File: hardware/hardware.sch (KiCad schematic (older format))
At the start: 1 part, among them P1 CONN_13X2

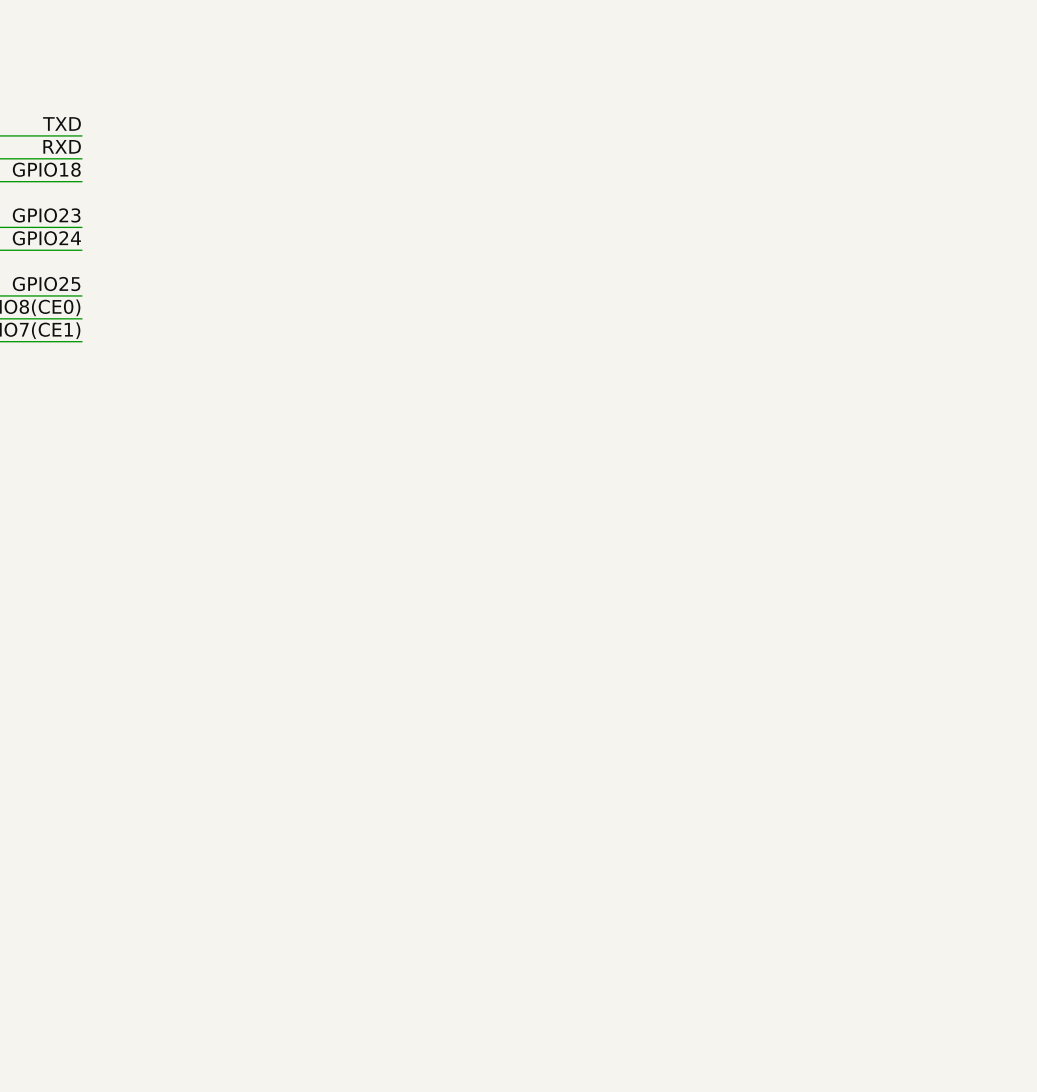
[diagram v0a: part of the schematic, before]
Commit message: Start daughterboard work
What I plan to do here is use the Pi's serial interface to provide the
position value for the servos and then use the other GPIO pins to provide
the selection for which motor is to move.

Signed-off-by: Nkeck720 <noahkeck72@gmail.com>
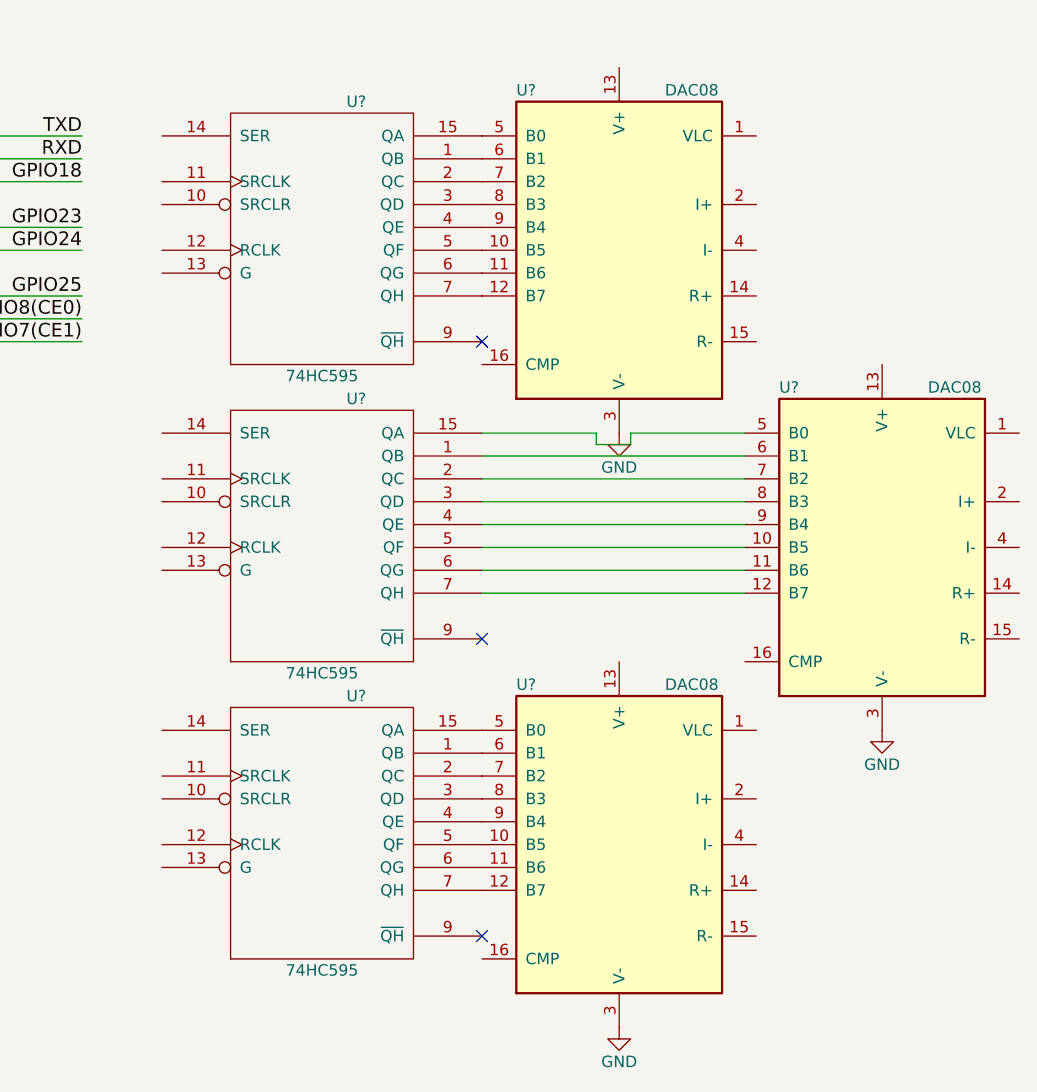
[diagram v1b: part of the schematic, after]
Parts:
- added U? (x3): 74HC595, symbol 74HC595
- added U? (x3): DAC08, symbol DAC08
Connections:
- net GND: now also U?.3 (V-), U?.3 (V-), U?.3 (V-), U?.8 (GND), U?.8 (GND), U?.8 (GND)
- new net: U?.1 (QB), U?.6 (B1) (x3)
- new net: U?.15 (QA), U?.5 (B0) (x3)
- new net: U?.2 (QC), U?.7 (B2) (x3)
- new net: U?.3 (QD), U?.8 (B3) (x3)
- new net: U?.4 (QE), U?.9 (B4) (x3)
- new net: U?.10 (B5), U?.5 (QF) (x3)
- new net: U?.11 (B6), U?.6 (QG) (x3)
- new net: U?.12 (B7), U?.7 (QH) (x3)
- new net VCC: U?.16 (VCC), U?.16 (VCC), U?.16 (VCC)
- no-connect marks 6 -> 9
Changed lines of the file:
@@
 Text GLabel 2900 1050 2    60   Input ~ 0
 +5
+$Comp
+L 74HC595 U?
+U 1 1 59263A27
+P 4550 1950
+F 0 "U?" H 4700 2550 50  0000 C CNN
+F 1 "74HC595" H 4550 1350 50  0000 C CNN
+F 2 "" H 4550 1950 50  0000 C CNN
+F 3 "" H 4550 1950 50  0000 C CNN
+	1    4550 1950
+	1    0    0    -1
+$EndComp
+$Comp
+L 74HC595 U?
+U 1 1 59263B0C
+P 4550 3250
+F 0 "U?" H 4700 3850 50  0000 C CNN
+F 1 "74HC595" H 4550 2650 50  0000 C CNN
+F 2 "" H 4550 3250 50  0000 C CNN
+F 3 "" H 4550 3250 50  0000 C CNN
+	1    4550 3250
+	1    0    0    -1
+$EndComp
+$Comp
+L 74HC595 U?
+U 1 1 59263BC3
+P 4550 4550
+F 0 "U?" H 4700 5150 50  0000 C CNN
+F 1 "74HC595" H 4550 3950 50  0000 C CNN
+F 2 "" H 4550 4550 50  0000 C CNN
+F 3 "" H 4550 4550 50  0000 C CNN
+	1    4550 4550
+	1    0    0    -1
+$EndComp
+$Comp
+L DAC08 U?
+U 1 1 59263EBB
+P 5850 2000
+F 0 "U?" H 5400 2700 50  0000 L CNN
+F 1 "DAC08" H 6050 2700 50  0000 L CNN
+F 2 "" H 5850 2000 50  0000 C CNN
+F 3 "" H 5850 2000 50  0000 C CNN
+	1    5850 2000
+	1    0    0    -1
+$EndComp
+$Comp
+L DAC08 U?
+U 1 1 592640B3
+P 7000 3300
+F 0 "U?" H 6550 4000 50  0000 L CNN
+F 1 "DAC08" H 7200 4000 50  0000 L CNN
+F 2 "" H 7000 3300 50  0000 C CNN
+F 3 "" H 7000 3300 50  0000 C CNN
+	1    7000 3300
+	1    0    0    -1
+$EndComp
+$Comp
+L DAC08 U?
+U 1 1 5926437E
+P 5850 4600
+F 0 "U?" H 5400 5300 50  0000 L CNN
+F 1 "DAC08" H 6050 5300 50  0000 L CNN
+F 2 "" H 5850 4600 50  0000 C CNN
+F 3 "" H 5850 4600 50  0000 C CNN
+	1    5850 4600
+	1    0    0    -1
+$EndComp
+Wire Wire Line
+	5250 2800 5750 2800
+Wire Wire Line
+	5750 2800 5750 2850
+Wire Wire Line
+	5750 2850 5900 2850
+Wire Wire Line
+	5900 2850 5900 2800
+Wire Wire Line
+	5900 2800 6400 2800
+Wire Wire Line
+	5250 2900 6400 2900
+Wire Wire Line
+	5250 3000 6400 3000
+Wire Wire Line
+	6400 3100 5250 3100
+Wire Wire Line
+	5250 3200 6400 3200
+Wire Wire Line
+	6400 3300 5250 3300
+Wire Wire Line
+	6400 3400 5250 3400
+Wire Wire Line
+	5250 3500 6400 3500
+$Comp
+L GND #PWR?
+U 1 1 59264B0C
+P 5850 2800
+F 0 "#PWR?" H 5850 2550 50  0001 C CNN
+F 1 "GND" H 5850 2650 50  0000 C CNN
+F 2 "" H 5850 2800 50  0000 C CNN
+F 3 "" H 5850 2800 50  0000 C CNN
+	1    5850 2800
+	1    0    0    -1
+$EndComp
+$Comp
+L GND #PWR?
+U 1 1 59264B9E
+P 7000 4100
+F 0 "#PWR?" H 7000 3850 50  0001 C CNN
+F 1 "GND" H 7000 3950 50  0000 C CNN
+F 2 "" H 7000 4100 50  0000 C CNN
+F 3 "" H 7000 4100 50  0000 C CNN
+	1    7000 4100
+	1    0    0    -1
+$EndComp
+$Comp
+L GND #PWR?
+U 1 1 59264C45
+P 5850 5400
+F 0 "#PWR?" H 5850 5150 50  0001 C CNN
+F 1 "GND" H 5850 5250 50  0000 C CNN
+F 2 "" H 5850 5400 50  0000 C CNN
+F 3 "" H 5850 5400 50  0000 C CNN
+	1    5850 5400
+	1    0    0    -1
+$EndComp
+NoConn ~ 5250 5000
+NoConn ~ 5250 3700
+NoConn ~ 5250 2400
 $EndSCHEMATC

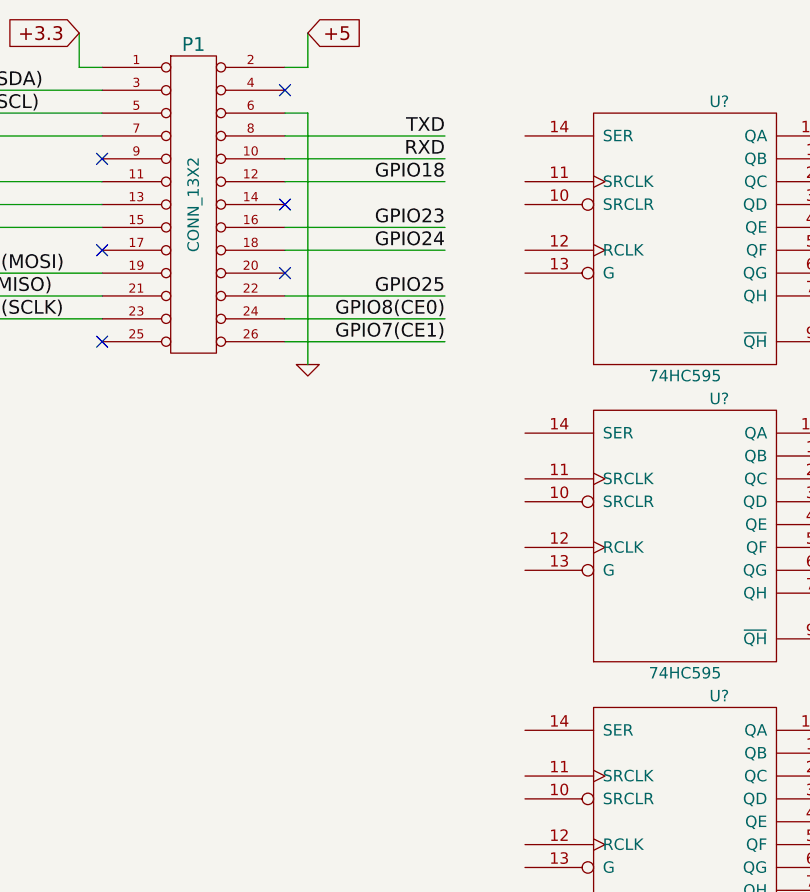
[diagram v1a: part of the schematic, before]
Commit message: Add serial outputs
Signed-off-by: Nkeck720 <noahkeck72@gmail.com>
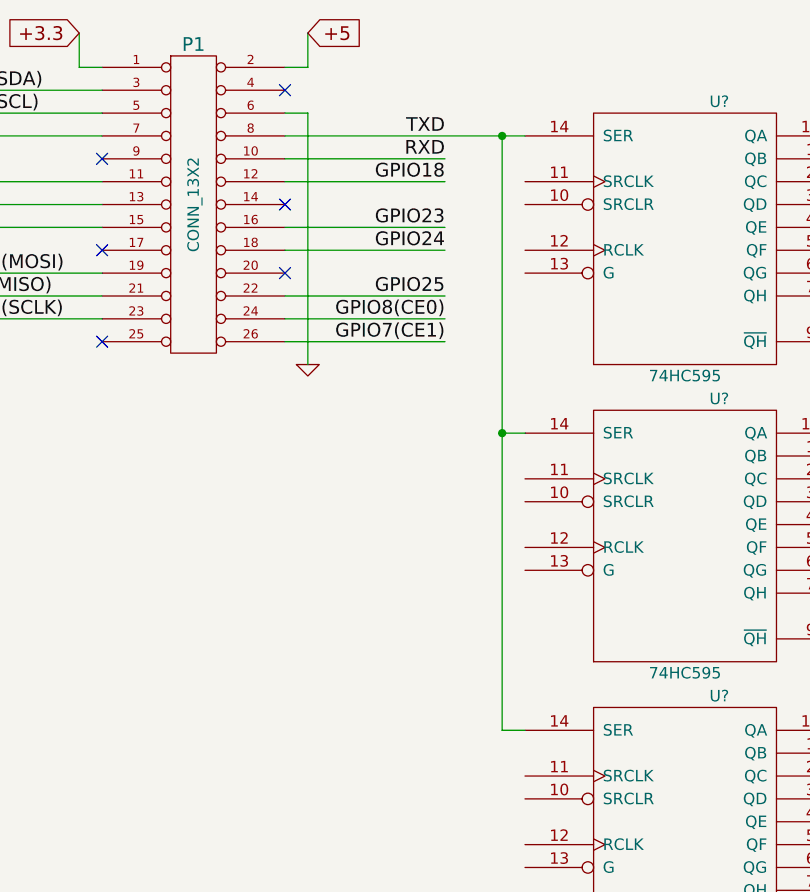
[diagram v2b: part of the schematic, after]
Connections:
- net TXD: now also U?.14 (SER), U?.14 (SER), U?.14 (SER)
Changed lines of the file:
@@
 	2900 1400 2800 1400
 Wire Wire Line
-	2800 1500 3500 1500
+	2800 1500 3850 1500
 Wire Wire Line
 	2800 1600 3500 1600
@@
 NoConn ~ 5250 3700
 NoConn ~ 5250 2400
+Wire Wire Line
+	3750 1500 3750 4100
+Wire Wire Line
+	3750 2800 3850 2800
+Connection ~ 3750 1500
+Wire Wire Line
+	3750 4100 3850 4100
+Connection ~ 3750 2800
 $EndSCHEMATC

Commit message: Finished hardware Rev. 1, see schematic.pdf
Signed-off-by: Nkeck720 <noahkeck72@gmail.com>
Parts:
- added C?: 0.01u, symbol C
- added C?: 10pF, symbol C
- added C?: 4.8 uF, symbol C
- added D?: 1N4007, symbol D
- added Q?: Q_NPN_BCE, symbol Q_NPN_BCE
- added R?: 5k6, symbol R
- added U?: LM555N, symbol LM555N
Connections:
- net labels added: OUT1
- wire segments 38 -> 65
- no-connect marks 9 -> 10
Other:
- note added: "Out to motor PWM pin"
- note added: "SCLK/RCLK needs to be set at 300 baud, will a 555 be stable enough or will\nwe need a crystal oscillator?"
- note added: "We will continue this pattern for each motor enable pin."
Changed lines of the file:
@@
 Wire Wire Line
 	5250 3500 6400 3500
-$Comp
-L GND #PWR?
-U 1 1 59264B0C
+NoConn ~ 5250 5000
+NoConn ~ 5250 3700
+NoConn ~ 5250 2400
+Wire Wire Line
+	3750 1500 3750 4100
+Wire Wire Line
+	3750 2800 3850 2800
+Connection ~ 3750 1500
+Wire Wire Line
+	3750 4100 3850 4100
+Connection ~ 3750 2800
+Text Notes 900  2850 0    60   ~ 0
+We will continue this pattern for each motor enable pin.
+$Comp
+L GND #PWR?
+U 1 1 592AEF1D
+P 6450 1500
+F 0 "#PWR?" H 6450 1250 50  0001 C CNN
+F 1 "GND" H 6450 1350 50  0000 C CNN
+F 2 "" H 6450 1500 50  0000 C CNN
+F 3 "" H 6450 1500 50  0000 C CNN
+	1    6450 1500
+	1    0    0    -1
+$EndComp
+NoConn ~ 6450 2000
+$Comp
+L C C?
+U 1 1 592AEFD0
+P 5250 2700
+F 0 "C?" H 5275 2800 50  0000 L CNN
+F 1 "0.01u" H 5275 2600 50  0000 L CNN
+F 2 "" H 5288 2550 50  0000 C CNN
+F 3 "" H 5250 2700 50  0000 C CNN
+	1    5250 2700
+	-1   0    0    1
+$EndComp
+Wire Wire Line
+	5250 2550 5250 2500
+Wire Wire Line
+	5250 2850 5650 2850
+Wire Wire Line
+	5650 2850 5650 2750
+Wire Wire Line
+	5650 2750 5800 2750
+Wire Wire Line
+	5800 2750 5800 2800
+Wire Wire Line
+	5800 2800 5850 2800
+Text GLabel 5850 1200 0    60   Input ~ 0
++5
+$Comp
+L GND #PWR?
+U 1 1 592AF253
 P 5850 2800
 F 0 "#PWR?" H 5850 2550 50  0001 C CNN
@@
 $EndComp
 $Comp
-L GND #PWR?
-U 1 1 59264B9E
-P 7000 4100
-F 0 "#PWR?" H 7000 3850 50  0001 C CNN
-F 1 "GND" H 7000 3950 50  0000 C CNN
-F 2 "" H 7000 4100 50  0000 C CNN
-F 3 "" H 7000 4100 50  0000 C CNN
-	1    7000 4100
-	1    0    0    -1
-$EndComp
-$Comp
-L GND #PWR?
-U 1 1 59264C45
-P 5850 5400
-F 0 "#PWR?" H 5850 5150 50  0001 C CNN
-F 1 "GND" H 5850 5250 50  0000 C CNN
-F 2 "" H 5850 5400 50  0000 C CNN
-F 3 "" H 5850 5400 50  0000 C CNN
-	1    5850 5400
-	1    0    0    -1
-$EndComp
-NoConn ~ 5250 5000
-NoConn ~ 5250 3700
-NoConn ~ 5250 2400
-Wire Wire Line
-	3750 1500 3750 4100
-Wire Wire Line
-	3750 2800 3850 2800
-Connection ~ 3750 1500
-Wire Wire Line
-	3750 4100 3850 4100
-Connection ~ 3750 2800
+L LM555N U?
+U 1 1 592AF521
+P 8050 1650
+F 0 "U?" H 7650 2000 50  0000 L CNN
+F 1 "LM555N" H 7650 1300 50  0000 L CNN
+F 2 "" H 8050 1650 50  0000 C CNN
+F 3 "" H 8050 1650 50  0000 C CNN
+	1    8050 1650
+	1    0    0    -1
+$EndComp
+Text GLabel 7350 1150 1    60   Input ~ 0
++5
+Wire Wire Line
+	7350 1150 7350 1850
+Wire Wire Line
+	7350 1850 7550 1850
+Wire Wire Line
+	8550 1850 8650 1850
+Wire Wire Line
+	8650 1850 8650 1950
+$Comp
+L C C?
+U 1 1 592AFA2F
+P 7500 2100
+F 0 "C?" H 7525 2200 50  0000 L CNN
+F 1 "10pF" H 7525 2000 50  0000 L CNN
+F 2 "" H 7538 1950 50  0000 C CNN
+F 3 "" H 7500 2100 50  0000 C CNN
+	1    7500 2100
+	1    0    0    -1
+$EndComp
+Wire Wire Line
+	7500 1950 7500 1650
+Wire Wire Line
+	7500 1650 7550 1650
+$Comp
+L GND #PWR?
+U 1 1 592AFABD
+P 7500 2250
+F 0 "#PWR?" H 7500 2000 50  0001 C CNN
+F 1 "GND" H 7500 2100 50  0000 C CNN
+F 2 "" H 7500 2250 50  0000 C CNN
+F 3 "" H 7500 2250 50  0000 C CNN
+	1    7500 2250
+	1    0    0    -1
+$EndComp
+$Comp
+L R R?
+U 1 1 592AFBB3
+P 9000 1800
+F 0 "R?" V 9080 1800 50  0000 C CNN
+F 1 "5k6" V 9000 1800 50  0000 C CNN
+F 2 "" V 8930 1800 50  0000 C CNN
+F 3 "" H 9000 1800 50  0000 C CNN
+	1    9000 1800
+	1    0    0    -1
+$EndComp
+$Comp
+L C C?
+U 1 1 592AFD03
+P 9000 2100
+F 0 "C?" H 9025 2200 50  0000 L CNN
+F 1 "4.8 uF" H 9025 2000 50  0000 L CNN
+F 2 "" H 9038 1950 50  0000 C CNN
+F 3 "" H 9000 2100 50  0000 C CNN
+	1    9000 2100
+	1    0    0    -1
+$EndComp
+$Comp
+L GND #PWR?
+U 1 1 592AFDB4
+P 9000 2250
+F 0 "#PWR?" H 9000 2000 50  0001 C CNN
+F 1 "GND" H 9000 2100 50  0000 C CNN
+F 2 "" H 9000 2250 50  0000 C CNN
+F 3 "" H 9000 2250 50  0000 C CNN
+	1    9000 2250
+	1    0    0    -1
+$EndComp
+Wire Wire Line
+	7550 1450 7250 1450
+Wire Wire Line
+	7250 1450 7250 2250
+Wire Wire Line
+	7250 2250 8750 2250
+Wire Wire Line
+	8750 1200 7350 1200
+Connection ~ 7350 1200
+Wire Wire Line
+	8550 1450 8550 1050
+Wire Wire Line
+	8550 1050 9600 1050
+Text GLabel 9600 1050 2    60   Input ~ 0
+OUT1
+$Comp
+L D D?
+U 1 1 592AFFFB
+P 8750 1800
+F 0 "D?" H 8750 1900 50  0000 C CNN
+F 1 "1N4007" H 8750 1700 50  0000 C CNN
+F 2 "" H 8750 1800 50  0000 C CNN
+F 3 "" H 8750 1800 50  0000 C CNN
+	1    8750 1800
+	0    -1   -1   0
+$EndComp
+Wire Wire Line
+	8650 1950 9000 1950
+Connection ~ 8750 1950
+Wire Wire Line
+	8550 1650 9000 1650
+Connection ~ 8750 1650
+Wire Wire Line
+	8750 2250 8750 1950
+$Comp
+L Q_NPN_BCE Q?
+U 1 1 592B0265
+P 8850 1400
+F 0 "Q?" H 8750 1600 50  0000 R CNN
+F 1 "Q_NPN_BCE" H 8750 1500 50  0000 R CNN
+F 2 "" H 9050 1500 50  0000 C CNN
+F 3 "" H 8850 1400 50  0000 C CNN
+	1    8850 1400
+	-1   0    0    -1
+$EndComp
+Wire Wire Line
+	8750 1600 8750 1650
+Wire Wire Line
+	9050 1400 9500 1400
+Wire Wire Line
+	9500 1400 9500 800
+Wire Wire Line
+	9500 800  6900 800
+Wire Wire Line
+	6900 800  6900 1800
+Wire Wire Line
+	6900 1800 6450 1800
+Text Notes 9500 1200 0    60   ~ 0
+Out to motor PWM pin
+Text Notes 700  5650 0    60   ~ 0
+SCLK/RCLK needs to be set at 300 baud, will a 555 be stable enough or will\nwe need a crystal oscillator?
 $EndSCHEMATC

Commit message: Annotate schematic
Signed-off-by: Nkeck720 <noahkeck72@gmail.com>
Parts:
- gave numbers to parts that had none: 13
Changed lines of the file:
@@
 NoConn ~ 2000 2400
 $Comp
-L GND-RESCUE-hardware #PWR03
+L GND-RESCUE-hardware #PWR1
 U 1 1 50A55C3F
 P 2900 2500
-F 0 "#PWR03" H 2900 2500 30  0001 C CNN
+F 0 "#PWR1" H 2900 2500 30  0001 C CNN
 F 1 "GND" H 2900 2430 30  0001 C CNN
 F 2 "" H 2900 2500 60  0001 C CNN
@@
 +5
 $Comp
-L 74HC595 U?
+L 74HC595 U1
 U 1 1 59263A27
 P 4550 1950
-F 0 "U?" H 4700 2550 50  0000 C CNN
+F 0 "U1" H 4700 2550 50  0000 C CNN
 F 1 "74HC595" H 4550 1350 50  0000 C CNN
 F 2 "" H 4550 1950 50  0000 C CNN
@@
 $EndComp
 $Comp
-L 74HC595 U?
+L 74HC595 U2
 U 1 1 59263B0C
 P 4550 3250
-F 0 "U?" H 4700 3850 50  0000 C CNN
+F 0 "U2" H 4700 3850 50  0000 C CNN
 F 1 "74HC595" H 4550 2650 50  0000 C CNN
 F 2 "" H 4550 3250 50  0000 C CNN
@@
 $EndComp
 $Comp
-L 74HC595 U?
+L 74HC595 U3
 U 1 1 59263BC3
 P 4550 4550
-F 0 "U?" H 4700 5150 50  0000 C CNN
+F 0 "U3" H 4700 5150 50  0000 C CNN
 F 1 "74HC595" H 4550 3950 50  0000 C CNN
 F 2 "" H 4550 4550 50  0000 C CNN
@@
 $EndComp
 $Comp
-L DAC08 U?
+L DAC08 U4
 U 1 1 59263EBB
 P 5850 2000
-F 0 "U?" H 5400 2700 50  0000 L CNN
+F 0 "U4" H 5400 2700 50  0000 L CNN
 F 1 "DAC08" H 6050 2700 50  0000 L CNN
 F 2 "" H 5850 2000 50  0000 C CNN
@@
 $EndComp
 $Comp
-L DAC08 U?
+L DAC08 U6
 U 1 1 592640B3
 P 7000 3300
-F 0 "U?" H 6550 4000 50  0000 L CNN
+F 0 "U6" H 6550 4000 50  0000 L CNN
 F 1 "DAC08" H 7200 4000 50  0000 L CNN
 F 2 "" H 7000 3300 50  0000 C CNN
@@
 $EndComp
 $Comp
-L DAC08 U?
+L DAC08 U5
 U 1 1 5926437E
 P 5850 4600
-F 0 "U?" H 5400 5300 50  0000 L CNN
+F 0 "U5" H 5400 5300 50  0000 L CNN
 F 1 "DAC08" H 6050 5300 50  0000 L CNN
 F 2 "" H 5850 4600 50  0000 C CNN
@@
 We will continue this pattern for each motor enable pin.
 $Comp
-L GND #PWR?
+L GND #PWR3
 U 1 1 592AEF1D
 P 6450 1500
-F 0 "#PWR?" H 6450 1250 50  0001 C CNN
+F 0 "#PWR3" H 6450 1250 50  0001 C CNN
 F 1 "GND" H 6450 1350 50  0000 C CNN
 F 2 "" H 6450 1500 50  0000 C CNN
@@
 NoConn ~ 6450 2000
 $Comp
-L C C?
+L C C1
 U 1 1 592AEFD0
 P 5250 2700
-F 0 "C?" H 5275 2800 50  0000 L CNN
+F 0 "C1" H 5275 2800 50  0000 L CNN
 F 1 "0.01u" H 5275 2600 50  0000 L CNN
 F 2 "" H 5288 2550 50  0000 C CNN
@@
 +5
 $Comp
-L GND #PWR?
+L GND #PWR2
 U 1 1 592AF253
 P 5850 2800
-F 0 "#PWR?" H 5850 2550 50  0001 C CNN
+F 0 "#PWR2" H 5850 2550 50  0001 C CNN
 F 1 "GND" H 5850 2650 50  0000 C CNN
 F 2 "" H 5850 2800 50  0000 C CNN
@@
 $EndComp
 $Comp
-L LM555N U?
+L LM555N U7
 U 1 1 592AF521
 P 8050 1650
-F 0 "U?" H 7650 2000 50  0000 L CNN
+F 0 "U7" H 7650 2000 50  0000 L CNN
 F 1 "LM555N" H 7650 1300 50  0000 L CNN
 F 2 "" H 8050 1650 50  0000 C CNN
@@
 	8650 1850 8650 1950
 $Comp
-L C C?
+L C C2
 U 1 1 592AFA2F
 P 7500 2100
-F 0 "C?" H 7525 2200 50  0000 L CNN
+F 0 "C2" H 7525 2200 50  0000 L CNN
 F 1 "10pF" H 7525 2000 50  0000 L CNN
 F 2 "" H 7538 1950 50  0000 C CNN
@@
 	7500 1650 7550 1650
 $Comp
-L GND #PWR?
+L GND #PWR4
 U 1 1 592AFABD
 P 7500 2250
-F 0 "#PWR?" H 7500 2000 50  0001 C CNN
+F 0 "#PWR4" H 7500 2000 50  0001 C CNN
 F 1 "GND" H 7500 2100 50  0000 C CNN
 F 2 "" H 7500 2250 50  0000 C CNN
@@
 $EndComp
 $Comp
-L R R?
+L R R1
 U 1 1 592AFBB3
 P 9000 1800
-F 0 "R?" V 9080 1800 50  0000 C CNN
+F 0 "R1" V 9080 1800 50  0000 C CNN
 F 1 "5k6" V 9000 1800 50  0000 C CNN
 F 2 "" V 8930 1800 50  0000 C CNN
@@
 $EndComp
 $Comp
-L C C?
+L C C3
 U 1 1 592AFD03
 P 9000 2100
-F 0 "C?" H 9025 2200 50  0000 L CNN
+F 0 "C3" H 9025 2200 50  0000 L CNN
 F 1 "4.8 uF" H 9025 2000 50  0000 L CNN
 F 2 "" H 9038 1950 50  0000 C CNN
@@
 $EndComp
 $Comp
-L GND #PWR?
+L GND #PWR5
 U 1 1 592AFDB4
 P 9000 2250
-F 0 "#PWR?" H 9000 2000 50  0001 C CNN
+F 0 "#PWR5" H 9000 2000 50  0001 C CNN
 F 1 "GND" H 9000 2100 50  0000 C CNN
 F 2 "" H 9000 2250 50  0000 C CNN
@@
 OUT1
 $Comp
-L D D?
+L D D1
 U 1 1 592AFFFB
 P 8750 1800
-F 0 "D?" H 8750 1900 50  0000 C CNN
+F 0 "D1" H 8750 1900 50  0000 C CNN
 F 1 "1N4007" H 8750 1700 50  0000 C CNN
 F 2 "" H 8750 1800 50  0000 C CNN
@@
 	8750 2250 8750 1950
 $Comp
-L Q_NPN_BCE Q?
+L Q_NPN_BCE Q1
 U 1 1 592B0265
 P 8850 1400
-F 0 "Q?" H 8750 1600 50  0000 R CNN
+F 0 "Q1" H 8750 1600 50  0000 R CNN
 F 1 "Q_NPN_BCE" H 8750 1500 50  0000 R CNN
 F 2 "" H 9050 1500 50  0000 C CNN
